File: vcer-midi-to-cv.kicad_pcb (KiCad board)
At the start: 4 copper layers, 140 x 128.5 mm, 109 parts, among them J1 Conn_01x10_Male, J10 CV3, J11 CV4, J12 Vel1, J13 Vel2, J14 Vel3, J15 Vel4, J16 Gate1, J17 Gate2, J18 Gate3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

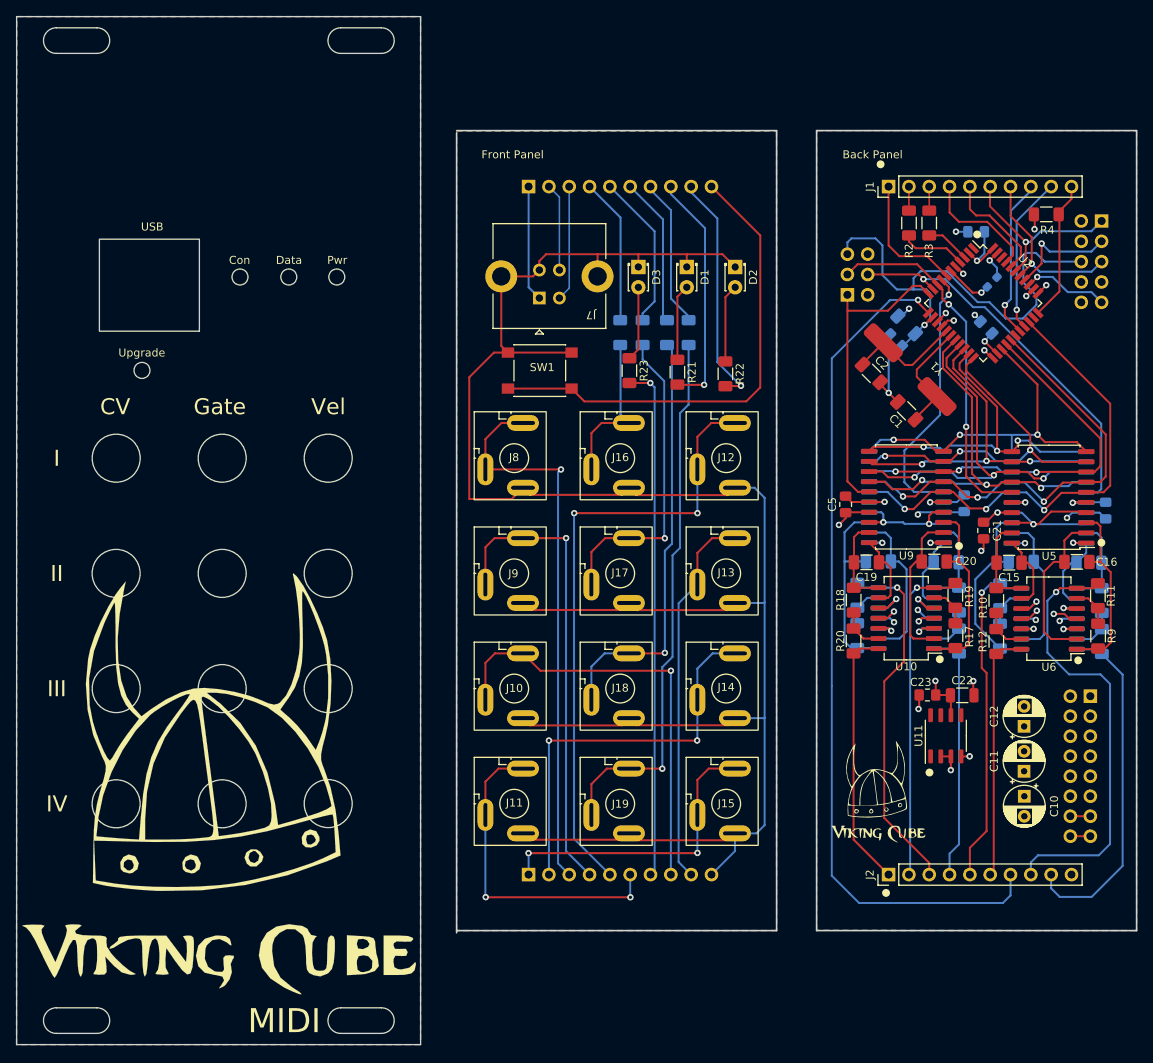
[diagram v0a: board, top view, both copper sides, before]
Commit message: removed other panels
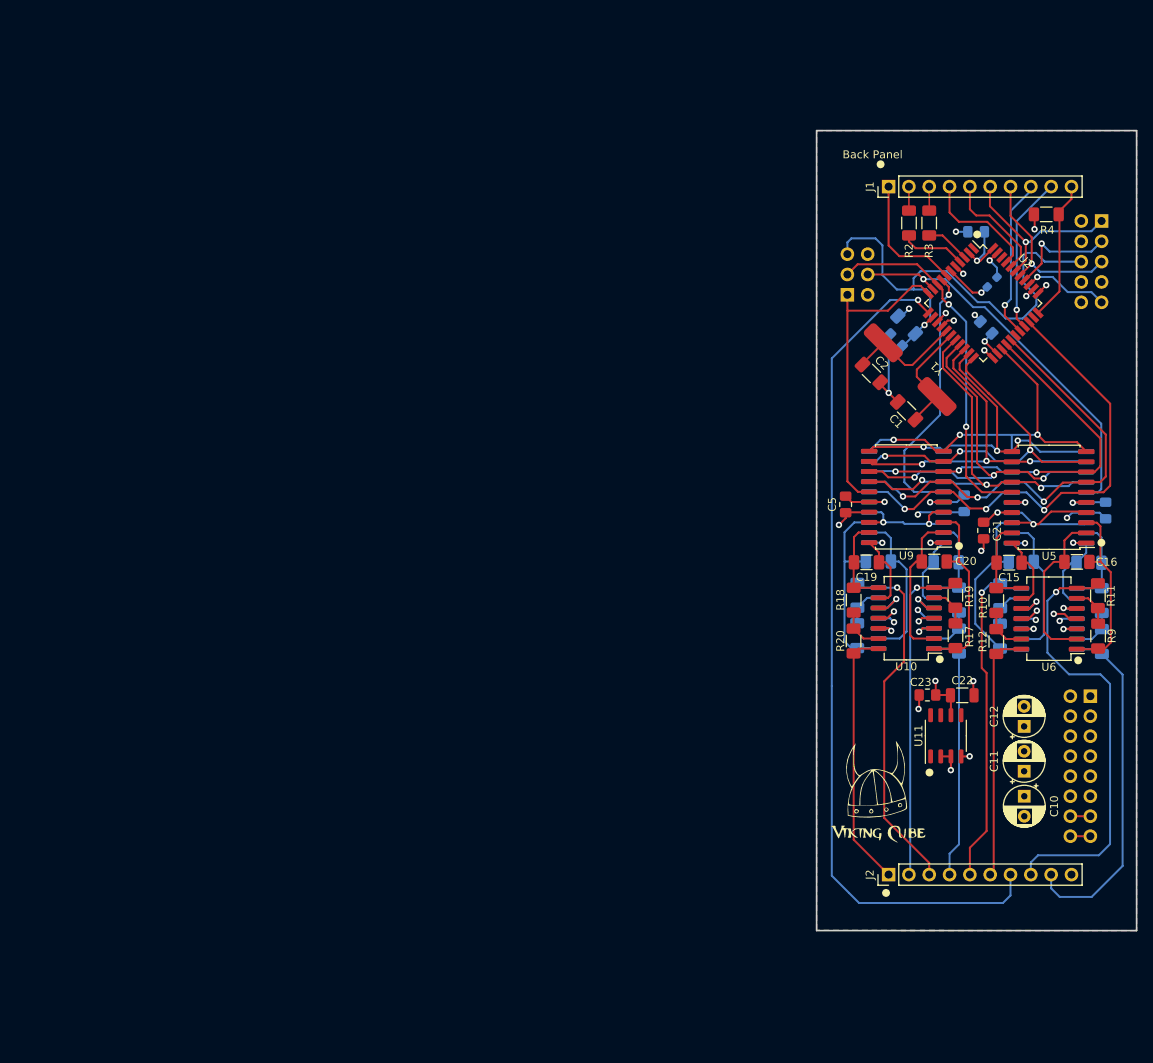
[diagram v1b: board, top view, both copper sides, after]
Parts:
- removed D1, D2, D3: LED, LED_THT:LED_D1.8mm_W3.3mm_H2.4mm
- removed the G*** at (-19.9, 89.7)
- removed the G*** at (6.69, 30.3)
- removed J10: CV3, eurorack:LUM 1502-03
- removed J11: CV4, eurorack:LUM 1502-03
- removed J12: Vel1, eurorack:LUM 1502-03
- removed J13: Vel2, eurorack:LUM 1502-03
- removed J14: Vel3, eurorack:LUM 1502-03
- removed J15: Vel4, eurorack:LUM 1502-03
- removed J16: Gate1, eurorack:LUM 1502-03
- removed J17: Gate2, eurorack:LUM 1502-03
- removed J18: Gate3, eurorack:LUM 1502-03
- removed J19: Gate4, eurorack:LUM 1502-03
- removed J7: USB_B, eurorack:USB-BG
- removed J8: CV1, eurorack:LUM 1502-03
- removed J9: CV2, eurorack:LUM 1502-03
- removed Mount_1, Mount_2, Mount_3, Mount_4: mounting, eurorack:mounting
- removed R21, R22, R23: R, Resistor_SMD:R_1206_3216Metric_Pad1.30x1.75mm_HandSolder
- removed REF1, REF10, REF11, REF12, REF2, REF3, REF4, REF5, REF6, REF7, REF8, REF9: mount_LUM_1502-03, eurorack:mount_LUM_1502-03
- removed REF13, REF14, REF15, REF16: mount_m2, eurorack:mount_m2
- removed REF17: mount_USB-BG, eurorack:mount_USB-BG
- removed SW1: Program, Button_Switch_SMD:SW_Push_1P1T_NO_6x6mm_H9.5mm
- removed locked (x4): 470, Resistor_SMD:R_1206_3216Metric_Pad1.30x1.75mm_HandSolder
- removed locked (x2): Conn_01x10_Female, Connector_PinSocket_2.54mm:PinSocket_1x10_P2.54mm_Vertical
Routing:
- net GND2: track 259.1 -> 0.00 mm
- net /fV1: track 77.4 -> 0.00 mm, vias 2 -> 0
- net /fCV1: track 70.1 -> 0.00 mm, vias 1 -> 0
- net Net-(J19-PadT): track 67.9 -> 0.00 mm, vias 1 -> 0
- net /fL3: track 64.5 -> 0.00 mm, vias 1 -> 0
- net /fPRG: track 60.5 -> 0.00 mm
- net /fCV2: track 58.5 -> 0.00 mm, vias 1 -> 0
- net /fCV3: track 54.7 -> 0.00 mm, vias 1 -> 0
- net Net-(J18-PadT): track 53.1 -> 0.00 mm, vias 1 -> 0
- net /fV3: track 49.8 -> 0.00 mm, vias 2 -> 0
- net /fV2: track 47.3 -> 0.00 mm
- net /fCV4: track 40.8 -> 0.00 mm, vias 2 -> 0
- net Net-(R25-Pad1): track 39.3 -> 0.00 mm, vias 1 -> 0
- net /fV4: track 38.2 -> 0.00 mm, vias 2 -> 0
- net /fL1: track 29.9 -> 0.00 mm, vias 1 -> 0
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- removed copper zone on B.Cu, net (none)
- removed copper zone on F.Cu, net (none)
- removed copper zone on B.Cu, net GND2
- removed copper zone on F.Cu, net GND2
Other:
- board size 140 x 128.5 mm -> 40 x 100 mm
- board text removed: "-55;0 [-50] 10HP"
- board text removed: "CV"
- board text removed: "Con"
- board text removed: "Data"
- board text removed: "Front Panel"
- board text removed: "Gate"
- board text removed: "I"
- board text removed: "II"
- board text removed: "III"
- board text removed: "IV"
- board text removed: "JLCJLCJLCJLC"
- board text removed: "MIDI"
- board text removed: "Pwr"
- board text removed: "USB"
- board text removed: "Upgrade"
- board text removed: "Vel"
